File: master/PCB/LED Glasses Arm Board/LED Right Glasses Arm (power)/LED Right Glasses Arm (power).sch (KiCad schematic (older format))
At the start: 24 parts, among them J1 Conn_01x02_Male, J2 Conn_01x01_Male, J3 Conn_01x01_Male, Q1 TP0610T, SW1 SW_SPST, U1 TPS63060

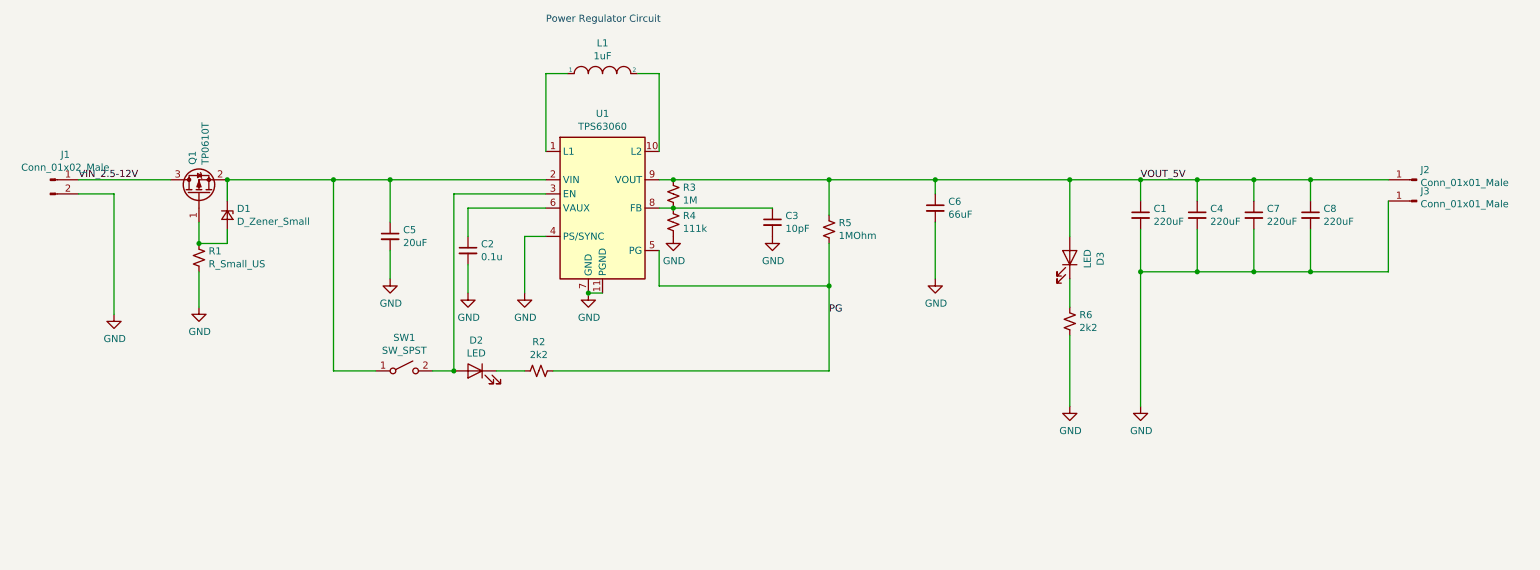
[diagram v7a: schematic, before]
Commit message: added parts for caps
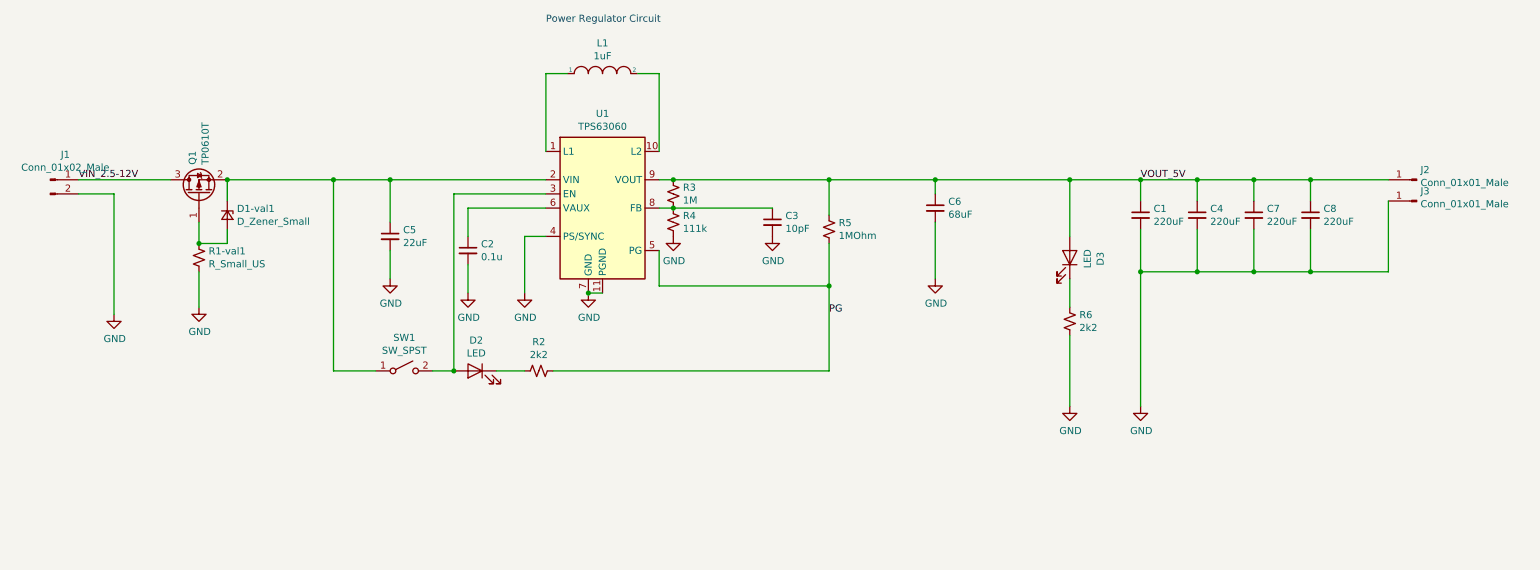
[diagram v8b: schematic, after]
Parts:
- C1, C4, C7, C8: footprint Capacitor_SMD:C_1206_3216Metric -> Capacitor_SMD:C_1210_3225Metric; Link https://au.element14.com/murata/grm31cr60j227me11l/cap-220-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 -> https://www.digikey.com.au/product-detail/en/samsung-electr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
- C2: footprint Capacitor_SMD:C_0603_1608Metric -> Capacitor_SMD:C_0402_1005Metric; Link (none) -> https://www.digikey.com.au/product-detail/en/samsung-electr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
- C3: Link (none) -> https://www.digikey.com.au/product-detail/en/avx-corporatio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
- C5: value 20uF -> 22uF; footprint Capacitor_SMD:C_0603_1608Metric -> Capacitor_SMD:C_0805_2012Metric; Link (none) -> https://www.digikey.com.au/product-detail/en/kemet/C0805C22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
- C6: value 66uF -> 68uF; footprint Capacitor_SMD:C_0603_1608Metric -> Capacitor_SMD:C_1206_3216Metric; Link (none) -> https://www.digikey.com.au/product-detail/en/tdk-corporatio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
- renumbered D1 to D1-val1, R1 to R1-val1
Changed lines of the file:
@@
 F 0 "C2" H 3892 4596 50  0000 L CNN
 F 1 "0.1u" H 3892 4505 50  0000 L CNN
-F 2 "Capacitor_SMD:C_0603_1608Metric" H 3800 4550 50  0001 C CNN
-F 3 "~" H 3800 4550 50  0001 C CNN
+F 2 "Capacitor_SMD:C_0402_1005Metric" H 3800 4550 50  0001 C CNN
+F 3 "https://media.digikey.com/pdf/Data%20Sheets/Samsung%20PDFs/CL05A104KA5NNNC.pdf" H 3800 4550 50  0001 C CNN
+F 4 "https://www.digikey.com.au/product-detail/en/samsung-electro-mechanics/CL05A104KA5NNNC/1276-1043-1-ND/3889129" H 3800 4550 50  0001 C CNN "Link"
 	1    3800 4550
 	1    0    0    -1
@@
 F 1 "10pF" H 6042 4305 50  0000 L CNN
 F 2 "Capacitor_SMD:C_0603_1608Metric" H 5950 4350 50  0001 C CNN
-F 3 "~" H 5950 4350 50  0001 C CNN
+F 3 "https://datasheets.avx.com/C0GNP0-Dielectric.pdf" H 5950 4350 50  0001 C CNN
+F 4 "https://www.digikey.com.au/product-detail/en/avx-corporation/06035A100JAT2A/478-1163-1-ND/564195" H 5950 4350 50  0001 C CNN "Link"
 	1    5950 4350
 	1    0    0    -1
@@
 	4400 5400 6350 5400
 $Comp
-L Device:D_Zener_Small D1
+L Device:D_Zener_Small D1-val1
 U 1 1 5F7F1725
 P 2100 4300
-F 0 "D1" V 2054 4368 50  0000 L CNN
+F 0 "D1-val1" V 2054 4368 50  0000 L CNN
 F 1 "D_Zener_Small" V 2145 4368 50  0000 L CNN
 F 2 "Diode_SMD:D_0603_1608Metric" V 2100 4300 50  0001 C CNN
@@
 $EndComp
 $Comp
-L Device:R_Small_US R1
+L Device:R_Small_US R1-val1
 U 1 1 5F7F24DD
 P 1900 4600
-F 0 "R1" H 1968 4646 50  0000 L CNN
+F 0 "R1-val1" H 1968 4646 50  0000 L CNN
 F 1 "R_Small_US" H 1968 4555 50  0000 L CNN
 F 2 "Resistor_SMD:R_0603_1608Metric" H 1900 4600 50  0001 C CNN
@@
 P 3250 4450
 F 0 "C5" H 3342 4496 50  0000 L CNN
-F 1 "20uF" H 3342 4405 50  0000 L CNN
-F 2 "Capacitor_SMD:C_0603_1608Metric" H 3250 4450 50  0001 C CNN
-F 3 "~" H 3250 4450 50  0001 C CNN
+F 1 "22uF" H 3342 4405 50  0000 L CNN
+F 2 "Capacitor_SMD:C_0805_2012Metric" H 3250 4450 50  0001 C CNN
+F 3 "https://content.kemet.com/datasheets/KEM_C1006_X5R_SMD.pdf" H 3250 4450 50  0001 C CNN
+F 4 "https://www.digikey.com.au/product-detail/en/kemet/C0805C226M9PAC7210/399-C0805C226M9PAC7210CT-ND/12701503" H 3250 4450 50  0001 C CNN "Link"
 	1    3250 4450
 	1    0    0    -1
@@
 P 7100 4250
 F 0 "C6" H 7192 4296 50  0000 L CNN
-F 1 "66uF" H 7192 4205 50  0000 L CNN
-F 2 "Capacitor_SMD:C_0603_1608Metric" H 7100 4250 50  0001 C CNN
-F 3 "~" H 7100 4250 50  0001 C CNN
+F 1 "68uF" H 7192 4205 50  0000 L CNN
+F 2 "Capacitor_SMD:C_1206_3216Metric" H 7100 4250 50  0001 C CNN
+F 3 "https://product.tdk.com/en/system/files?file=dam/doc/product/capacitor/ceramic/mlcc/catalog/mlcc_commercial_general_en.pdf" H 7100 4250 50  0001 C CNN
+F 4 "https://www.digikey.com.au/product-detail/en/tdk-corporation/C3216JB1A686M160AC/445-11687-1-ND/3953353" H 7100 4250 50  0001 C CNN "Link"
 	1    7100 4250
 	1    0    0    -1
@@
 F 0 "C1" H 8642 4346 50  0000 L CNN
 F 1 "220uF" H 8642 4255 50  0000 L CNN
-F 2 "Capacitor_SMD:C_1206_3216Metric" H 8550 4300 50  0001 C CNN
-F 3 "http://www.farnell.com/datasheets/2867879.pdf" H 8550 4300 50  0001 C CNN
-F 4 "https://au.element14.com/murata/grm31cr60j227me11l/cap-220-f-6-3v-20-x5r-1206/dp/2494472" H 8550 4300 50  0001 C CNN "Link"
+F 2 "Capacitor_SMD:C_1210_3225Metric" H 8550 4300 50  0001 C CNN
+F 3 "~" H 8550 4300 50  0001 C CNN
+F 4 "https://www.digikey.com.au/product-detail/en/samsung-electro-mechanics/CL32A227MQVNNNE/1276-3375-1-ND/3891461" H 8550 4300 50  0001 C CNN "Link"
 	1    8550 4300
 	1    0    0    -1
@@
 	10300 4700 10300 4200
 Connection ~ 8550 4700
+Wire Wire Line
+	8550 4700 8950 4700
+Wire Wire Line
+	8950 4400 8950 4700
+Connection ~ 8950 4700
+Wire Wire Line
+	8950 4700 9350 4700
+Wire Wire Line
+	9350 4400 9350 4700
+Connection ~ 9350 4700
+Wire Wire Line
+	9350 4700 9750 4700
+Wire Wire Line
+	9750 4400 9750 4700
+Connection ~ 9750 4700
+Wire Wire Line
+	9750 4700 10300 4700
+Wire Wire Line
+	8550 4050 8950 4050
 $Comp
 L Device:C_Small C4
-U 1 1 60562E44
+U 1 1 60699D26
 P 8950 4300
 F 0 "C4" H 9042 4346 50  0000 L CNN
 F 1 "220uF" H 9042 4255 50  0000 L CNN
-F 2 "Capacitor_SMD:C_1206_3216Metric" H 8950 4300 50  0001 C CNN
-F 3 "http://www.farnell.com/datasheets/2867879.pdf" H 8950 4300 50  0001 C CNN
-F 4 "https://au.element14.com/murata/grm31cr60j227me11l/cap-220-f-6-3v-20-x5r-1206/dp/2494472" H 8950 4300 50  0001 C CNN "Link"
+F 2 "Capacitor_SMD:C_1210_3225Metric" H 8950 4300 50  0001 C CNN
+F 3 "~" H 8950 4300 50  0001 C CNN
+F 4 "https://www.digikey.com.au/product-detail/en/samsung-electro-mechanics/CL32A227MQVNNNE/1276-3375-1-ND/3891461" H 8950 4300 50  0001 C CNN "Link"
 	1    8950 4300
 	1    0    0    -1
@@
 $Comp
 L Device:C_Small C7
-U 1 1 605639D8
+U 1 1 6069AB23
 P 9350 4300
 F 0 "C7" H 9442 4346 50  0000 L CNN
 F 1 "220uF" H 9442 4255 50  0000 L CNN
-F 2 "Capacitor_SMD:C_1206_3216Metric" H 9350 4300 50  0001 C CNN
-F 3 "http://www.farnell.com/datasheets/2867879.pdf" H 9350 4300 50  0001 C CNN
-F 4 "https://au.element14.com/murata/grm31cr60j227me11l/cap-220-f-6-3v-20-x5r-1206/dp/2494472" H 9350 4300 50  0001 C CNN "Link"
+F 2 "Capacitor_SMD:C_1210_3225Metric" H 9350 4300 50  0001 C CNN
+F 3 "~" H 9350 4300 50  0001 C CNN
+F 4 "https://www.digikey.com.au/product-detail/en/samsung-electro-mechanics/CL32A227MQVNNNE/1276-3375-1-ND/3891461" H 9350 4300 50  0001 C CNN "Link"
 	1    9350 4300
 	1    0    0    -1
@@
 $Comp
 L Device:C_Small C8
-U 1 1 60564591
+U 1 1 6069B97B
 P 9750 4300
 F 0 "C8" H 9842 4346 50  0000 L CNN
 F 1 "220uF" H 9842 4255 50  0000 L CNN
-F 2 "Capacitor_SMD:C_1206_3216Metric" H 9750 4300 50  0001 C CNN
-F 3 "http://www.farnell.com/datasheets/2867879.pdf" H 9750 4300 50  0001 C CNN
-F 4 "https://au.element14.com/murata/grm31cr60j227me11l/cap-220-f-6-3v-20-x5r-1206/dp/2494472" H 9750 4300 50  0001 C CNN "Link"
+F 2 "Capacitor_SMD:C_1210_3225Metric" H 9750 4300 50  0001 C CNN
+F 3 "~" H 9750 4300 50  0001 C CNN
+F 4 "https://www.digikey.com.au/product-detail/en/samsung-electro-mechanics/CL32A227MQVNNNE/1276-3375-1-ND/3891461" H 9750 4300 50  0001 C CNN "Link"
 	1    9750 4300
 	1    0    0    -1
 $EndComp
 Wire Wire Line
-	8550 4700 8950 4700
-Wire Wire Line
-	8550 4050 8950 4050
-Wire Wire Line
-	8950 4200 8950 4050
+	8950 4050 8950 4200
 Connection ~ 8950 4050
 Wire Wire Line
 	8950 4050 9350 4050
-Wire Wire Line
-	8950 4400 8950 4700
-Connection ~ 8950 4700
-Wire Wire Line
-	8950 4700 9350 4700
 Wire Wire Line
 	9350 4200 9350 4050
@@
 	9350 4050 9750 4050
 Wire Wire Line
-	9750 4200 9750 4050
+	9750 4050 9750 4200
 Connection ~ 9750 4050
 Wire Wire Line
 	9750 4050 10300 4050
-Wire Wire Line
-	9350 4400 9350 4700
-Connection ~ 9350 4700
-Wire Wire Line
-	9350 4700 9750 4700
-Wire Wire Line
-	9750 4400 9750 4700
-Connection ~ 9750 4700
-Wire Wire Line
-	9750 4700 10300 4700
 $EndSCHEMATC
